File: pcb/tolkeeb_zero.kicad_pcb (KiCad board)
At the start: 2 copper layers, 272.7 x 132.7 mm, 116 parts

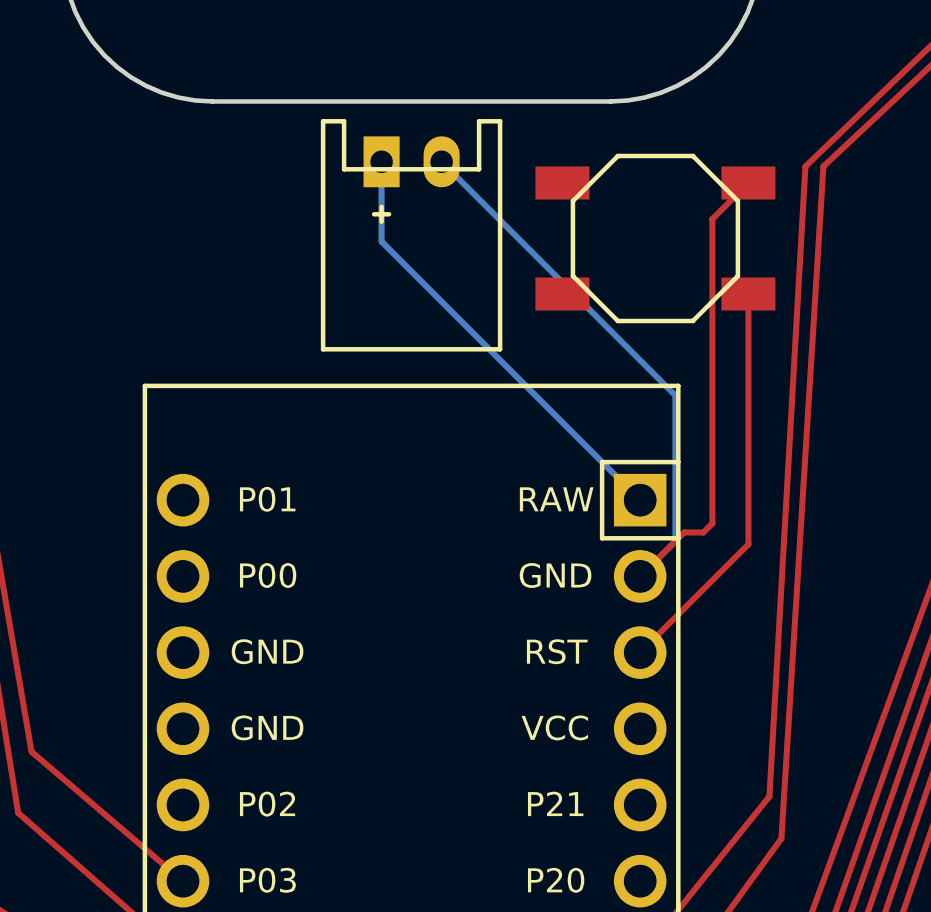
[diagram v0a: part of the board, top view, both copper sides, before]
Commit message: chore: minimal fixes based on DRC warnings
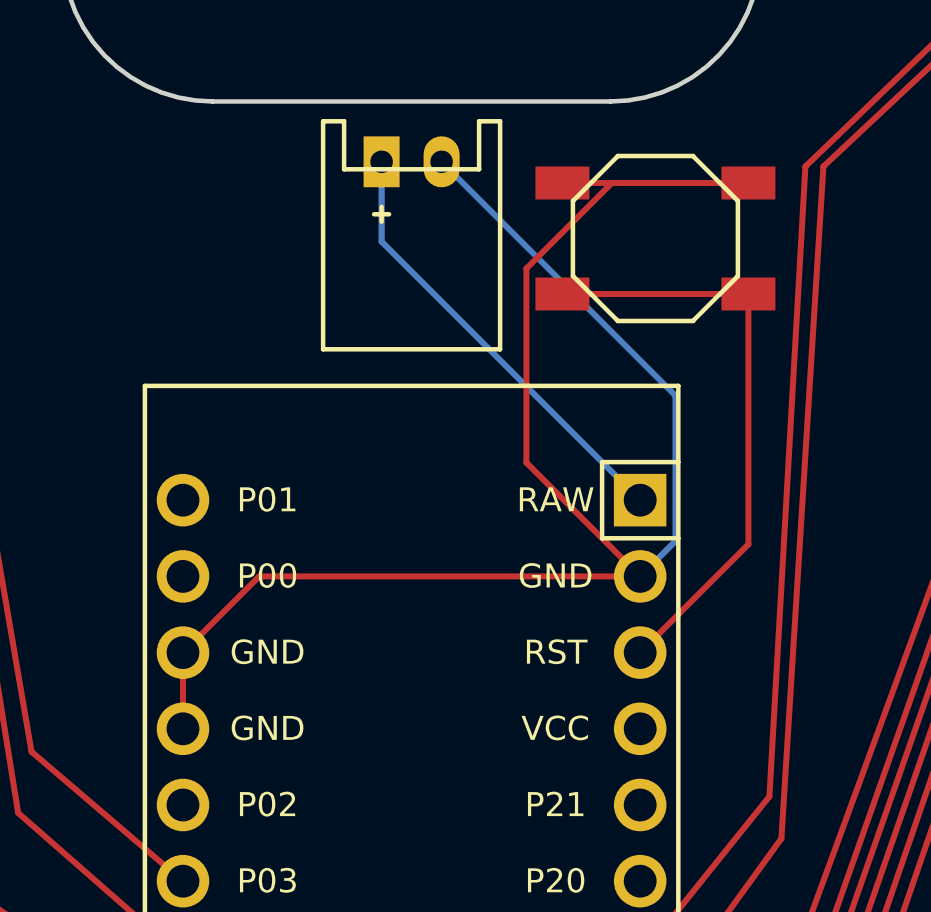
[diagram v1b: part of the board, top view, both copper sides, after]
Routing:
- net GND: track 32.5 -> 59.0 mm
- net RST: track 13.4 -> 19.6 mm

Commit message: feat: add gerbers export 😳
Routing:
- net P19: track 207.3 -> 206.3 mm, vias 4 -> 5
- net P15: track 189.8 -> 189.5 mm, vias 4 -> 6
- added copper zone on B.Cu, net GND
- added copper zone on F.Cu, net GND
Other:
- copper layers 2 -> 4
- rule pad_to_mask_clearance: 0.05 -> 0
